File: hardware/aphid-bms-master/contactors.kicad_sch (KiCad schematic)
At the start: 2 parts, among them U6 DRV8803

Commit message: Assigned some footprints
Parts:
- R8: footprint (none) -> Resistor_SMD:R_0805_2012Metric
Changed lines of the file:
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@@
 			)
 		)
-		(property "Footprint" ""
+		(property "Footprint" "Resistor_SMD:R_0805_2012Metric"
 			(at 98.298 95.25 90)
 			(effects

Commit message: Worked on BMS master
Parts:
- added C26, C27: 10uF 25V, Capacitor_SMD:C_0805_2012Metric, symbol Device:C
- added C28: 100nF, Capacitor_SMD:C_0805_2012Metric, symbol Device:C
- added D4: D_Schottky, Diode_SMD:D_SOD-123, symbol Device:D_Schottky
- added L5: 3.3uH, Inductor_SMD:L_Bourns_SRN8040TA, symbol Device:L
- added R10, R11: R, Resistor_SMD:R_0805_2012Metric, symbol Device:R
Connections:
- net CONTACTOR_NEG+: now also U6.1 (VM), U6.2 (VCLAMP), C26.1, C27.1, L5.2, R10.1
- net HVIL_SENSE: now also C28.1, R10.2, R11.1
- net GND: now reaches U6.14 (GND)
- net GND: now also U6.15 (GND), U6.16 (GND), U6.5 (GND), U6.6 (GND), U6.7 (GND), C26.2, C27.2, C28.2, R11.2
- new net: D4.1 (K), L5.1
- new net HVIL: D4.2 (A)
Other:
- note added: "TODO: Add voltage divider calculatiuon here"
- note removed: "Should this be driven by HVIL or +12V?"
- company: (none) -> https://aphid-ev.se
- title: (none) -> Aphid BMS Master

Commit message: Worked on BMS master layout
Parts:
- D4: footprint Diode_SMD:D_SOD-123 -> Diode_SMD:D_SMC; symbol Device:D_Schottky -> Diode:B340
- U6: footprint Package_SO:SOIC-16W_7.5x12.8mm_P1.27mm -> Package_SO:SOIC-20W_7.5x12.8mm_P1.27mm
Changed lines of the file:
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@@
 			)
 		)
-		(property "Footprint" "Package_SO:SOIC-16W_7.5x12.8mm_P1.27mm"
+		(property "Footprint" "Package_SO:SOIC-20W_7.5x12.8mm_P1.27mm"
 			(at 143.51 92.71 0)
 			(effects
@@
 	)
 	(symbol
-		(lib_id "Device:D_Schottky")
+		(lib_id "Diode:B340")
 		(at 45.72 36.83 180)
 		(unit 1)
@@
 			)
 		)
-		(property "Footprint" "Diode_SMD:D_SOD-123"
+		(property "Footprint" "Diode_SMD:D_SMC"
+			(at 45.72 32.385 0)
+			(effects
+				(font
+					(size 1.27 1.27)
+				)
+				(hide yes)
+			)
+		)
+		(property "Datasheet" "http://www.jameco.com/Jameco/Products/ProdDS/1538777.pdf"
 			(at 45.72 36.83 0)
 			(effects
@@
 			)
 		)
-		(property "Datasheet" "~"
+		(property "Description" "40V 3A Schottky Barrier Rectifier Diode, SMC"
 			(at 45.72 36.83 0)
 			(effects
-				(font
-					(size 1.27 1.27)
-				)
-				(hide yes)
-			)
-		)
-		(property "Description" "Schottky diode"
-			(at 45.72 36.83 0)
-			(effects

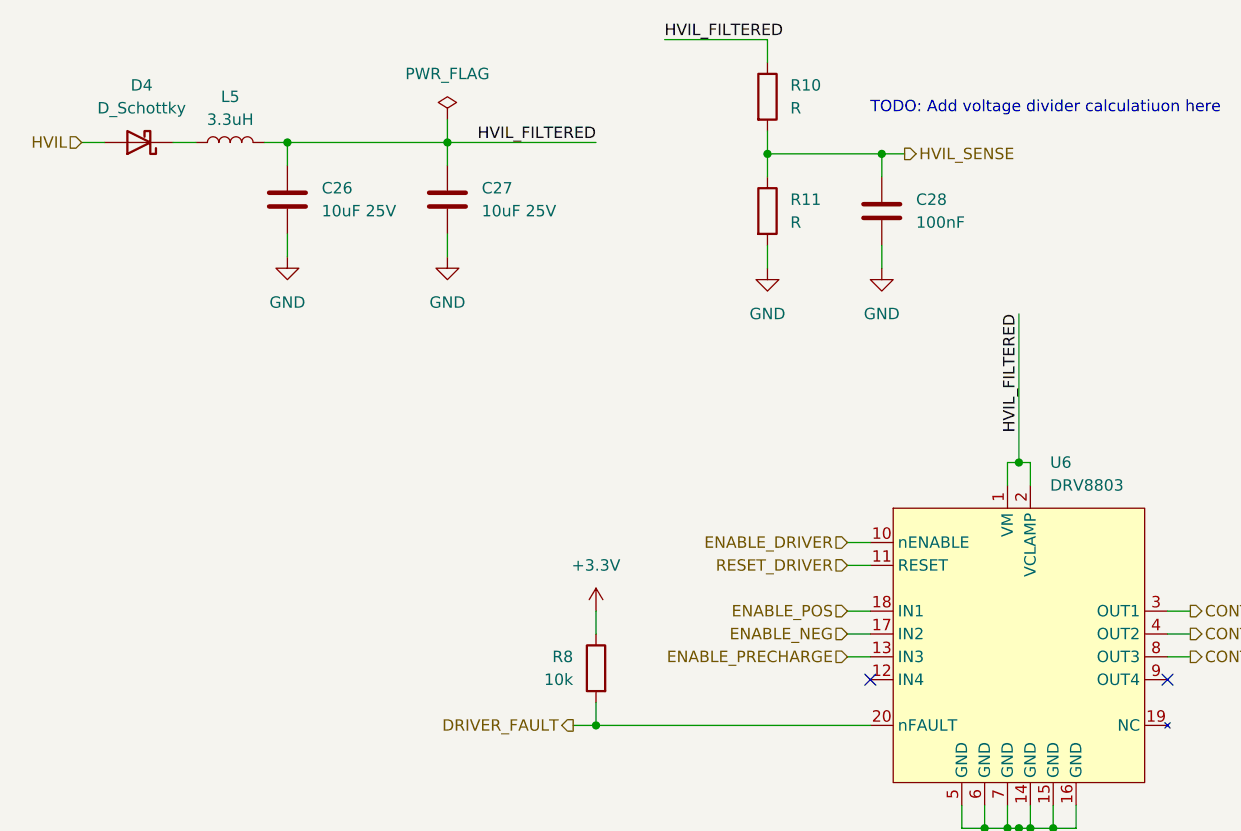
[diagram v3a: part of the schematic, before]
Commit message: Changed BMS Master to use MAX17851 instead of isolated CAN
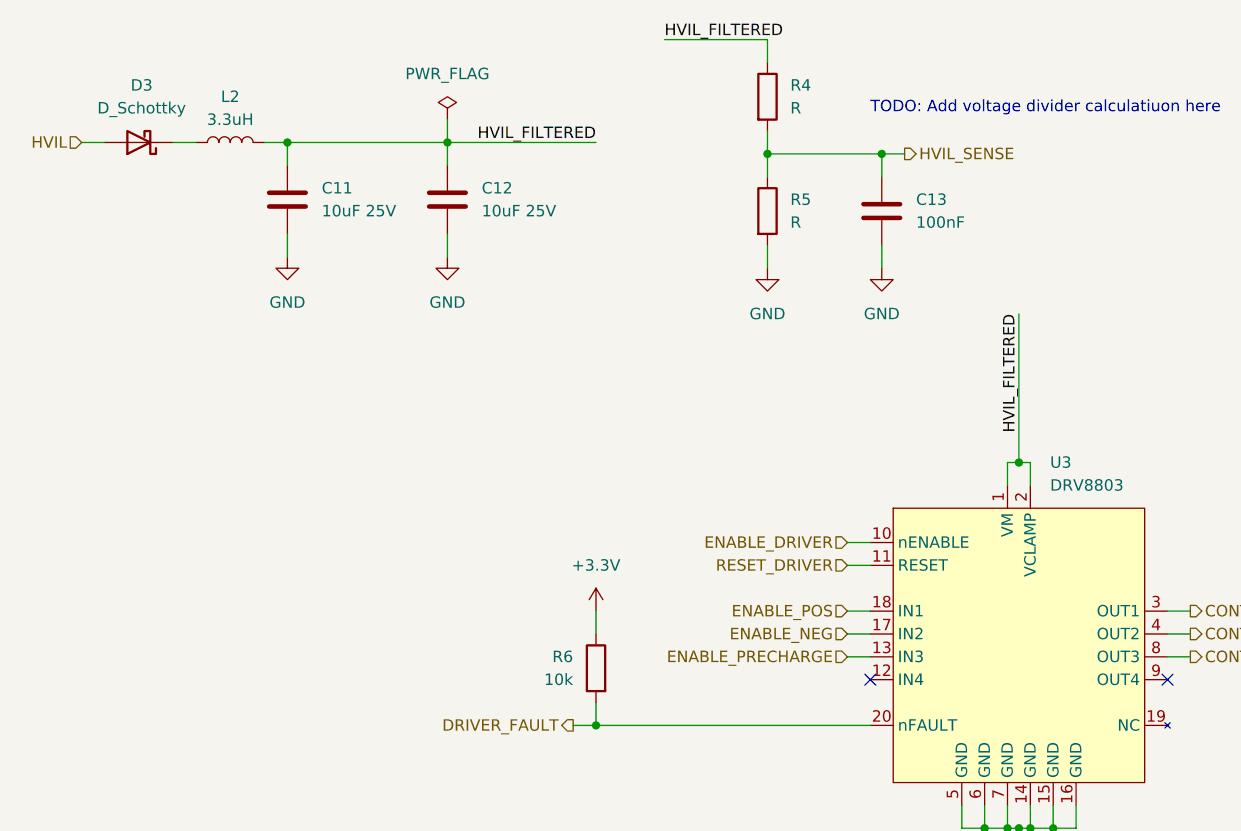
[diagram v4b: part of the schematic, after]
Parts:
- renumbered C26 to C11, C27 to C12, C28 to C13, D4 to D3, L5 to L2, R10 to R4, R11 to R5, R8 to R6, U6 to U3
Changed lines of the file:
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@@
 		(dnp no)
 		(fields_autoplaced yes)
-		(property "Reference" "U6"
+		(property "Reference" "U3"
 			(at 146.9741 72.39 0)
 			(effects
@@
 			(project ""
 				(path "/3fe4475e-7771-42d3-a39b-bb1b5919e27e/d4efc436-fbd4-4b7f-83cb-a124aea1dc9d"
-					(reference "U6")
+					(reference "U3")
 					(unit 1)
 				)
@@
 		(dnp no)
 		(fields_autoplaced yes)
-		(property "Reference" "#PWR063"
+		(property "Reference" "#PWR032"
 			(at 62.23 55.88 0)
 			(effects
@@
 			(project "aphid-bms-master"
 				(path "/3fe4475e-7771-42d3-a39b-bb1b5919e27e/d4efc436-fbd4-4b7f-83cb-a124aea1dc9d"
-					(reference "#PWR063")
+					(reference "#PWR032")
 					(unit 1)
 				)
@@
 		(dnp no)
 		(fields_autoplaced yes)
-		(property "Reference" "L5"
+		(property "Reference" "L2"
 			(at 55.88 31.75 90)
 			(effects
@@
 			(project "aphid-bms-master"
 				(path "/3fe4475e-7771-42d3-a39b-bb1b5919e27e/d4efc436-fbd4-4b7f-83cb-a124aea1dc9d"
-					(reference "L5")
+					(reference "L2")
 					(unit 1)
 				)
@@
 		(dnp no)
 		(fields_autoplaced yes)
-		(property "Reference" "R11"
+		(property "Reference" "R5"
 			(at 118.11 43.1799 0)
 			(effects
@@
 			(project "aphid-bms-master"
 				(path "/3fe4475e-7771-42d3-a39b-bb1b5919e27e/d4efc436-fbd4-4b7f-83cb-a124aea1dc9d"
-					(reference "R11")
+					(reference "R5")
 					(unit 1)
 				)
@@
 		(on_board yes)
 		(dnp no)
-		(property "Reference" "R8"
+		(property "Reference" "R6"
 			(at 93.98 93.9799 0)
 			(effects
@@
 			(project ""
 				(path "/3fe4475e-7771-42d3-a39b-bb1b5919e27e/d4efc436-fbd4-4b7f-83cb-a124aea1dc9d"
-					(reference "R8")
+					(reference "R6")
 					(unit 1)
 				)
@@
 		(dnp no)
 		(fields_autoplaced yes)
-		(property "Reference" "#PWR067"
+		(property "Reference" "#PWR034"
 			(at 115.57 57.15 0)
 			(effects
@@
 			(project "aphid-bms-master"
 				(path "/3fe4475e-7771-42d3-a39b-bb1b5919e27e/d4efc436-fbd4-4b7f-83cb-a124aea1dc9d"
-					(reference "#PWR067")
+					(reference "#PWR034")
 					(unit 1)
 				)
@@
 		(dnp no)
 		(fields_autoplaced yes)
-		(property "Reference" "C27"
+		(property "Reference" "C12"
 			(at 83.82 41.9099 0)
 			(effects
@@
 			(project "aphid-bms-master"
 				(path "/3fe4475e-7771-42d3-a39b-bb1b5919e27e/d4efc436-fbd4-4b7f-83cb-a124aea1dc9d"
-					(reference "C27")
+					(reference "C12")
 					(unit 1)
 				)
@@
 		(dnp no)
 		(fields_autoplaced yes)
-		(property "Reference" "#PWR065"
+		(property "Reference" "#PWR033"
 			(at 80.01 55.88 0)
 			(effects
@@
 			(project "aphid-bms-master"
 				(path "/3fe4475e-7771-42d3-a39b-bb1b5919e27e/d4efc436-fbd4-4b7f-83cb-a124aea1dc9d"
-					(reference "#PWR065")
+					(reference "#PWR033")
 					(unit 1)
 				)
@@
 		(dnp no)
 		(fields_autoplaced yes)
-		(property "Reference" "C26"
+		(property "Reference" "C11"
 			(at 66.04 41.9099 0)
 			(effects
@@
 			(project "aphid-bms-master"
 				(path "/3fe4475e-7771-42d3-a39b-bb1b5919e27e/d4efc436-fbd4-4b7f-83cb-a124aea1dc9d"
-					(reference "C26")
+					(reference "C11")
 					(unit 1)
 				)
@@
 		(dnp no)
 		(fields_autoplaced yes)
-		(property "Reference" "D4"
+		(property "Reference" "D3"
 			(at 46.0375 30.48 0)
 			(effects
@@
 			(project "aphid-bms-master"
 				(path "/3fe4475e-7771-42d3-a39b-bb1b5919e27e/d4efc436-fbd4-4b7f-83cb-a124aea1dc9d"
-					(reference "D4")
+					(reference "D3")
 					(unit 1)
 				)
@@
 		(dnp no)
 		(fields_autoplaced yes)
-		(property "Reference" "R10"
+		(property "Reference" "R4"
 			(at 118.11 30.4799 0)
 			(effects
@@
 			(project "aphid-bms-master"
 				(path "/3fe4475e-7771-42d3-a39b-bb1b5919e27e/d4efc436-fbd4-4b7f-83cb-a124aea1dc9d"
-					(reference "R10")
+					(reference "R4")
 					(unit 1)
 				)
@@
 		(dnp no)
 		(fields_autoplaced yes)
-		(property "Reference" "#PWR064"
+		(property "Reference" "#PWR037"
 			(at 143.51 121.92 0)
 			(effects
@@
 			(project "aphid-bms-master"
 				(path "/3fe4475e-7771-42d3-a39b-bb1b5919e27e/d4efc436-fbd4-4b7f-83cb-a124aea1dc9d"
-					(reference "#PWR064")
+					(reference "#PWR037")
 					(unit 1)
 				)
@@
 		(dnp no)
 		(fields_autoplaced yes)
-		(property "Reference" "C28"
+		(property "Reference" "C13"
 			(at 132.08 43.1799 0)
 			(effects
@@
 			(project "aphid-bms-master"
 				(path "/3fe4475e-7771-42d3-a39b-bb1b5919e27e/d4efc436-fbd4-4b7f-83cb-a124aea1dc9d"
-					(reference "C28")
+					(reference "C13")
 					(unit 1)
 				)
@@
 		(dnp no)
 		(fields_autoplaced yes)
-		(property "Reference" "#PWR068"
+		(property "Reference" "#PWR035"
 			(at 128.27 57.15 0)
 			(effects
@@
 			(project "aphid-bms-master"
 				(path "/3fe4475e-7771-42d3-a39b-bb1b5919e27e/d4efc436-fbd4-4b7f-83cb-a124aea1dc9d"
-					(reference "#PWR068")
+					(reference "#PWR035")
 					(unit 1)
 				)
@@
 		(dnp no)
 		(fields_autoplaced yes)
-		(property "Reference" "#FLG05"
+		(property "Reference" "#FLG02"
 			(at 80.01 32.385 0)
 			(effects
@@
 			(project ""
 				(path "/3fe4475e-7771-42d3-a39b-bb1b5919e27e/d4efc436-fbd4-4b7f-83cb-a124aea1dc9d"
-					(reference "#FLG05")
+					(reference "#FLG02")
 					(unit 1)
 				)
@@
 		(dnp no)
 		(fields_autoplaced yes)
-		(property "Reference" "#PWR035"
+		(property "Reference" "#PWR036"
 			(at 96.52 92.71 0)
 			(effects
@@
 			(project ""
 				(path "/3fe4475e-7771-42d3-a39b-bb1b5919e27e/d4efc436-fbd4-4b7f-83cb-a124aea1dc9d"
-					(reference "#PWR035")
-					(unit 1)
-				)
+					(reference "#PWR036")
+					(unit 1)
+				)

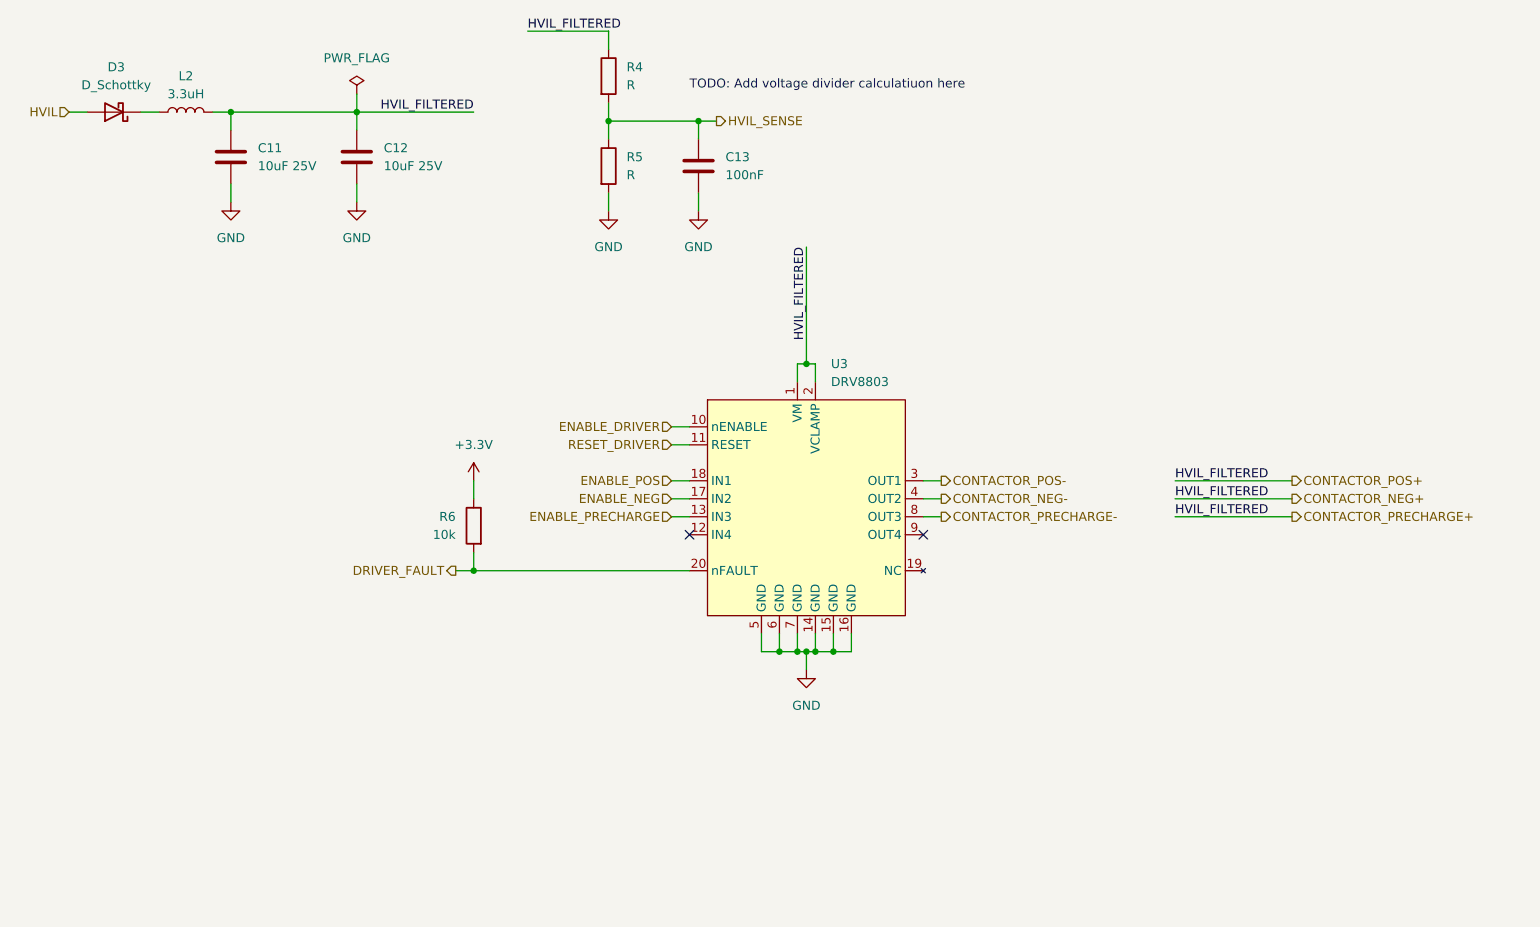
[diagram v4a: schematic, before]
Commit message: Harmonized VC and BMS components
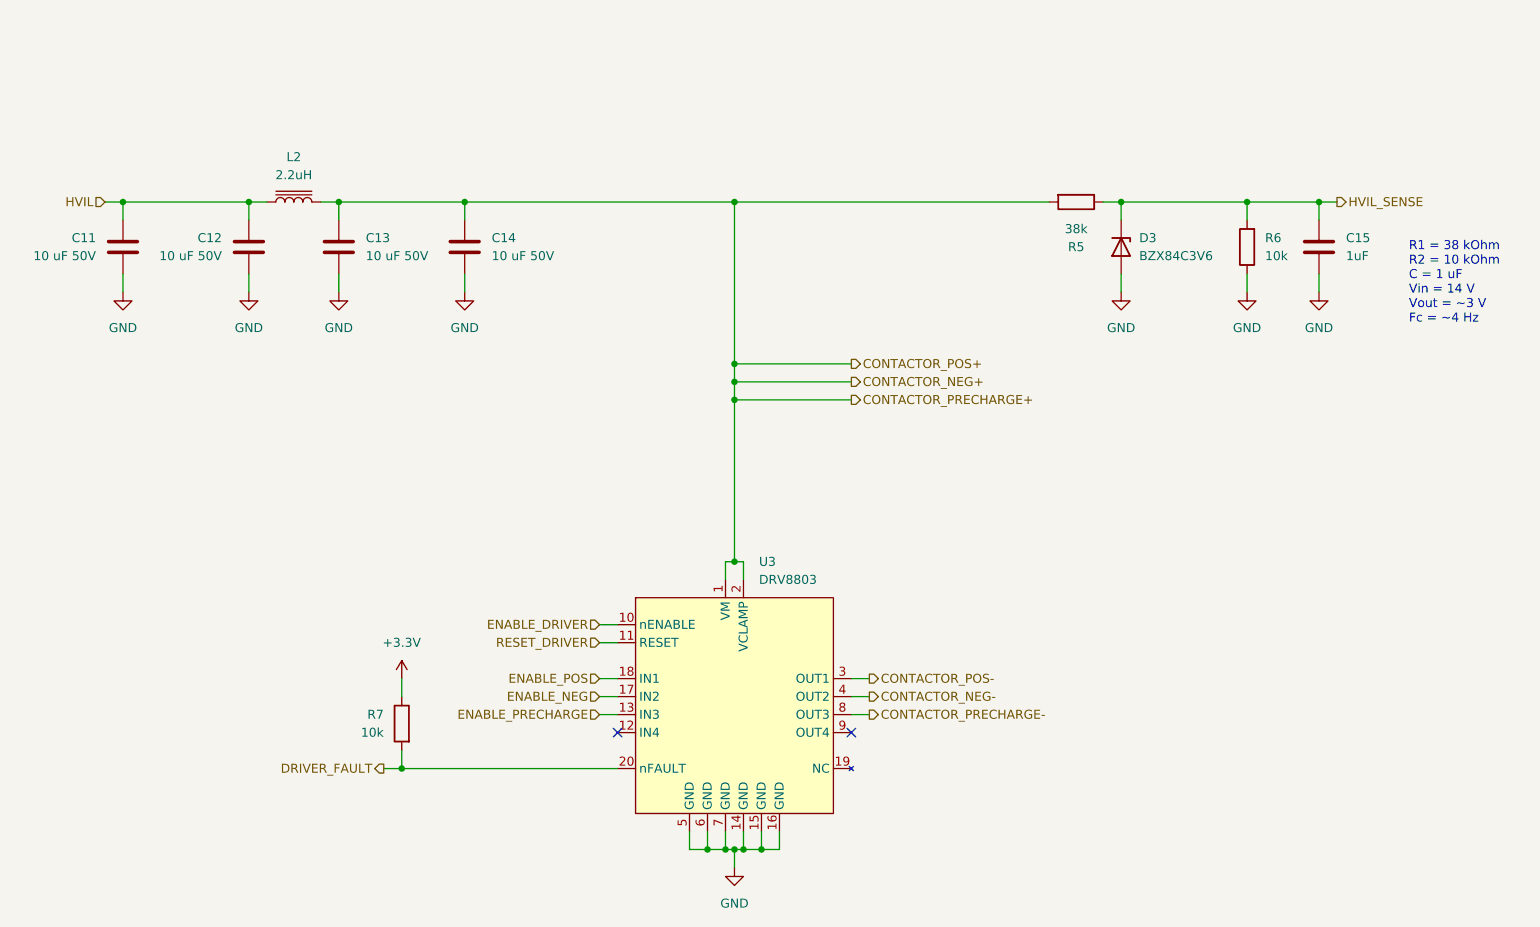
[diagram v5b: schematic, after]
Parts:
- removed D3: D_Schottky, Diode_SMD:D_SMC, symbol Diode:B340
- removed L2: 3.3uH, Inductor_SMD:L_Bourns_SRN8040TA, symbol Device:L
- removed R4: R, Resistor_SMD:R_0805_2012Metric, symbol Device:R
- added C14: 10 uF 50V, Capacitor_SMD:C_1206_3216Metric, symbol Device:C
- added C15: 1uF, Capacitor_SMD:C_0603_1608Metric, symbol Device:C
- added D3: BZX84C3V6, Package_TO_SOT_SMD:SOT-23, symbol Diode:BZX84Cxx
- added L2: 2.2uH, Inductor_SMD:L_Bourns_SRN8040TA, symbol Device:L_Iron
- added R6: 10k, Resistor_SMD:R_0603_1608Metric, symbol Device:R
- C11, C12: value 10uF 25V -> 10 uF 50V; footprint Capacitor_SMD:C_0805_2012Metric -> Capacitor_SMD:C_1206_3216Metric
- C13: value 100nF -> 10 uF 50V; footprint Capacitor_SMD:C_0805_2012Metric -> Capacitor_SMD:C_1206_3216Metric
- R5: value R -> 38k; footprint Resistor_SMD:R_0805_2012Metric -> Resistor_SMD:R_0603_1608Metric
- U3: footprint Package_SO:SOIC-20W_7.5x12.8mm_P1.27mm -> Package_SO:HTSSOP-16-1EP_4.4x5mm_P0.65mm_EP3.4x5mm_Mask3x3mm_ThermalVias
- renumbered R6 to R7
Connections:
- net CONTACTOR_NEG+: now also C13.1, R5.2, C14.1, L2.2; no longer C11.1, C12.1
- net GND: now also C14.2, C15.2, D3.1 (A), R6.1; no longer R5.2
- net HVIL: now also C11.1, C12.1, L2.1
- net HVIL_SENSE: now also C15.1, D3.3 (K), R6.2; no longer C13.1
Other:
- note added: "R1 = 38 kOhm R2 = 10 kOhm C = 1 uF Vin = 14 V Vout = ~3 V Fc = ~4 Hz"
- note removed: "TODO: Add voltage divider calculatiuon here"
- moved on the sheet: R7, U3
